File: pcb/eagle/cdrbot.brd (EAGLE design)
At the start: 50 x 50 mm, 28 parts, among them IC1 PIC18F25K50, J1 CON_HEADER_1X06-PTH_M, J12 ICSP, J13 CON_HEADER_1X05-PTH_M, J2 CON_HEADER_1X06-PTH_M, J3 CON_HEADER_1X06-PTH_M, J4 CON_HEADER_1X08-PTH_M, J5 CON_HEADER_1X08-PTH_M, J6 CON_HEADER_1X08-PTH_M, J7 CON_HEADER_1X03-PTH_M, J8 CON_HEADER_1X03-PTH_M, J9 CON_HEADER_1X03-PTH_M, SW1 RESET, SW2 PRG, X1 VIN

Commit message: Nueva version del PCB
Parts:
- removed J7, J8, J9: CON_HEADER_1X03-PTH_M, gary:M1X03_M
- removed JP1: USB-MICROB, SparkFun-Connectors:USB-MICROB
- removed X1: VIN, con-wago-508:W237-132
- added BATERIA, SWITCH: CON_HEADER_1X02-PTH-M, gary:M1X02_M
- added C4, C5: 22pF, gary:C025-025X050
- added SJ1: VBUS, jumper:SJ
- added XTAL1: 20MHz, gary:HC-49UV
- moved C1 5.57 mm to (12.7, 20.3), turned to 180 degrees
- moved R3 4.83 mm to (15.0, 38.1)
- moved ON 3.42 mm to (7.37, 39.1)
- moved RC0 3.30 mm to (18.5, 2.54)
- moved R4 1.37 mm to (18.5, 10.2)
- moved C2 1.27 mm to (32.5, 16.5)
- moved USB1 0.76 mm to (45.2, 13.2)
- moved C3 0.76 mm to (25.4, 1.78)
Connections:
- removed net RA6: IC1.10, J13.4
- removed net RA7: IC1.9, R2.1, SW2.2
- removed net RC1: IC1.12, J9.2
- new net N$2: BATERIA.1, SWITCH.2
- new net OSC1: C5.1, IC1.9, XTAL1.1
- new net OSC2: C4.1, IC1.10, XTAL1.2
- new net VBUS: SJ1.2, USB1.VUSB
- net 5V: now also SJ1.1, SWITCH.1; no longer J8.1, J8.2, J8.3, JP1.VBUS, USB1.VUSB, X1.1
- net D+: no longer JP1.D+
- net D-: no longer JP1.D-
- net GND: now also BATERIA.2, C4.2, C5.2; no longer J7.1, J7.2, J7.3, JP1.GND, JP1.MT1, JP1.MT2, X1.2
- net RB4: now also R2.1, SW2.2
- net RC0: no longer J9.3
- net RC2: now also J13.4; no longer J9.1
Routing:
- net RA7: track 46.3 -> 0.00 mm, vias 2 -> 0
- net GND: track 77.4 -> 39.6 mm, vias 6 -> 22
- net RA6: track 24.2 -> 0.00 mm
- net RB4: track 5.08 -> 24.9 mm
- net OSC1: track 0.00 -> 18.0 mm
- net OSC2: track 0.00 -> 12.1 mm
- net RC2: track 5.08 -> 16.5 mm
- net 5V: track 114.1 -> 105.9 mm
- net D-: track 32.2 -> 26.9 mm
- net RC1: track 5.08 -> 0.00 mm
- net VBUS: track 0.00 -> 3.43 mm
- net PIC_RX: track 19.7 -> 17.0 mm
- net N$2: track 0.00 -> 2.54 mm
- net D+: track 21.3 -> 23.2 mm, vias 2 -> 0
- net RC0: track 5.08 -> 3.57 mm
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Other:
- board text added: "20130507"
- board text removed: "20130423"
- board text removed: "RA6"
- board text removed: "RC0"
- board text removed: "RC1"
- board text removed: "VDD"
- board text removed: "VSS"

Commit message: Generados gerbers para fabricación
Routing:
- net GND: track 39.6 -> 38.3 mm
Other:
- board text added: "CdR"

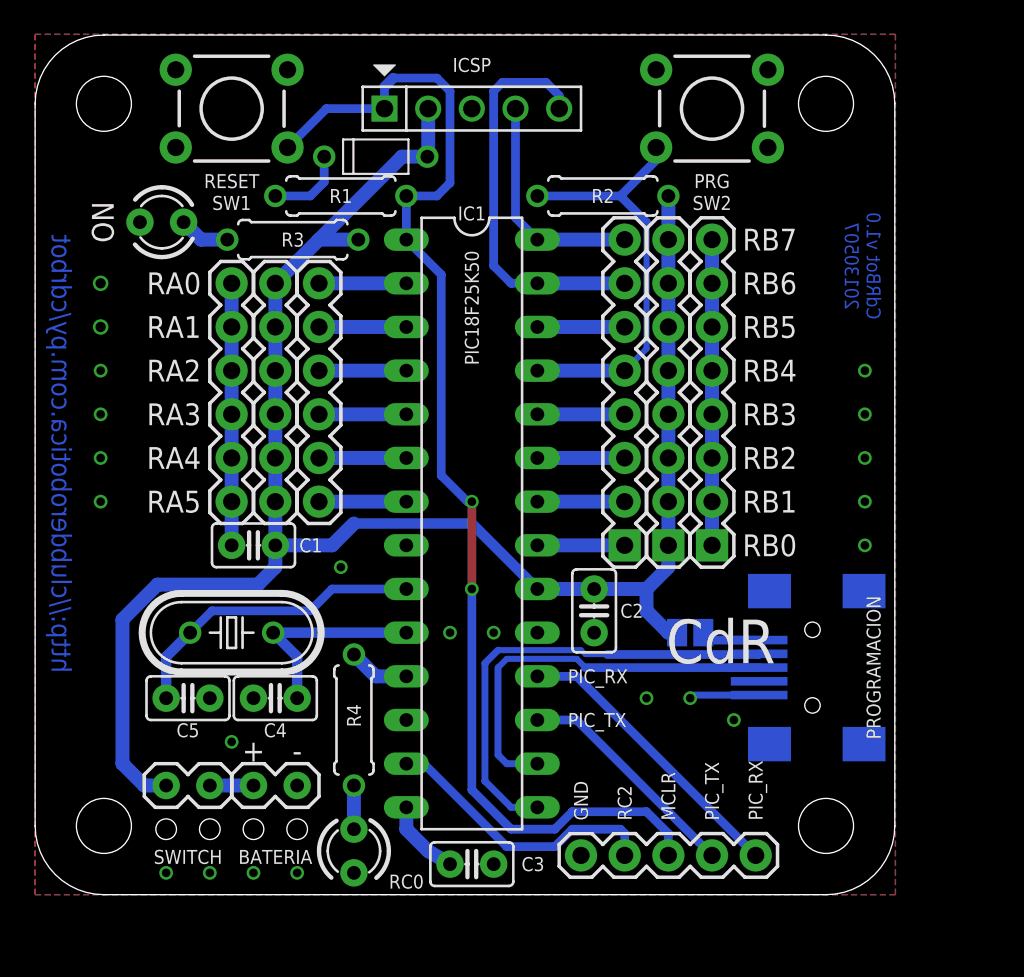
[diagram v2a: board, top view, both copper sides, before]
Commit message: Added On/Off switch, increase cable holes, removed diode
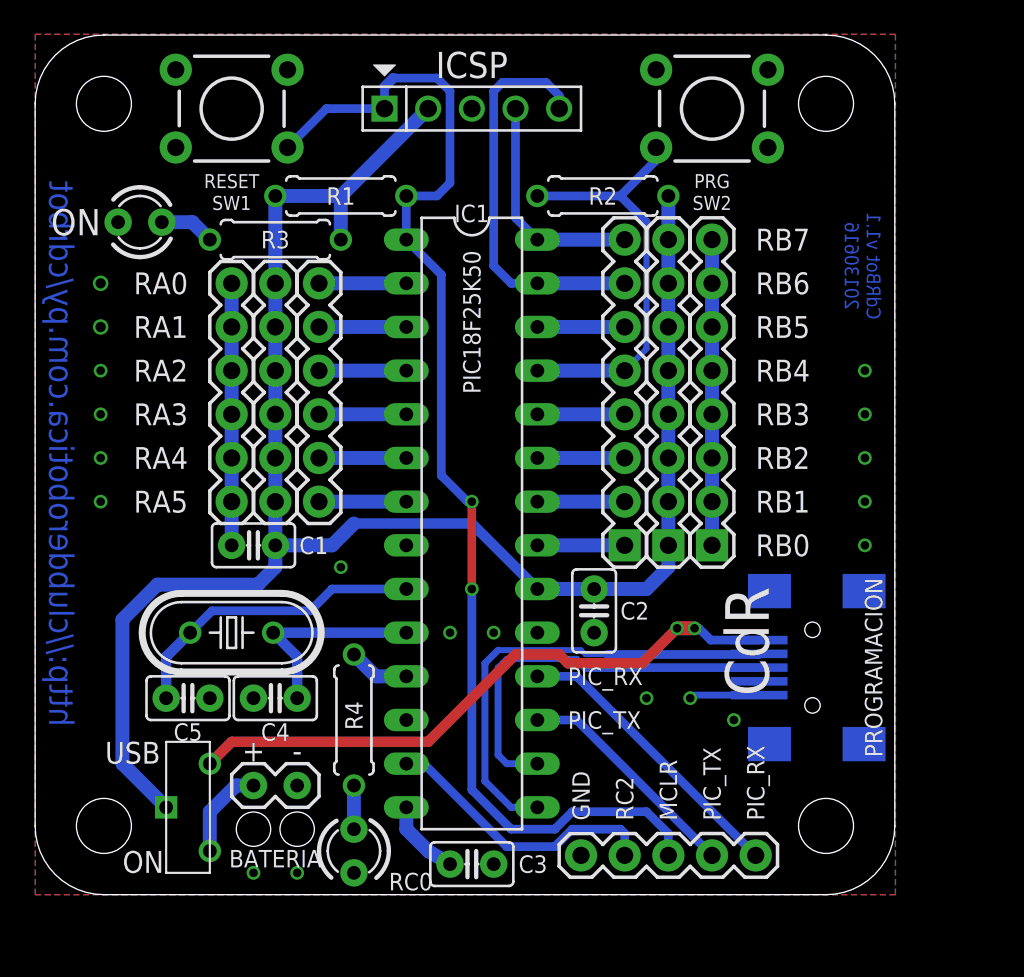
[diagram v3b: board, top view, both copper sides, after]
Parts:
- removed D1: 1N4148, SparkFun:DOIDE-1N4148
- removed SJ1: VBUS, jumper:SJ
- removed SWITCH: CON_HEADER_1X02-PTH-M, gary:M1X02_M
- added S1: 1P2T, gary:1P2T
- moved ON 1.27 mm to (6.10, 39.1)
- moved R3 1.02 mm to (14.0, 38.1)
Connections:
- removed net N$2: BATERIA.1, SWITCH.2
- net 5V: now also R1.2, S1.P$1; no longer D1.A, SJ1.1, SWITCH.1
- net N$1: now also BATERIA.1, S1.P$2; no longer D1.C, R1.2
- net VBUS: now also S1.P$3; no longer SJ1.2
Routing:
- net VBUS: track 3.43 -> 36.9 mm, vias 0 -> 2
- net N$2: track 2.54 -> 0.00 mm
- net 5V: track 105.9 -> 104.5 mm
- net N$1: track 4.65 -> 5.46 mm
- net GND: vias 22 -> 19
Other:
- board text added: "20130616"
- board text added: "CdRBot v1.1"
- board text added: "ON"
- board text added: "USB"
- board text removed: "20130507"
- board text removed: "CdRBot v1.0"

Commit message: Added support fot TSOP38238
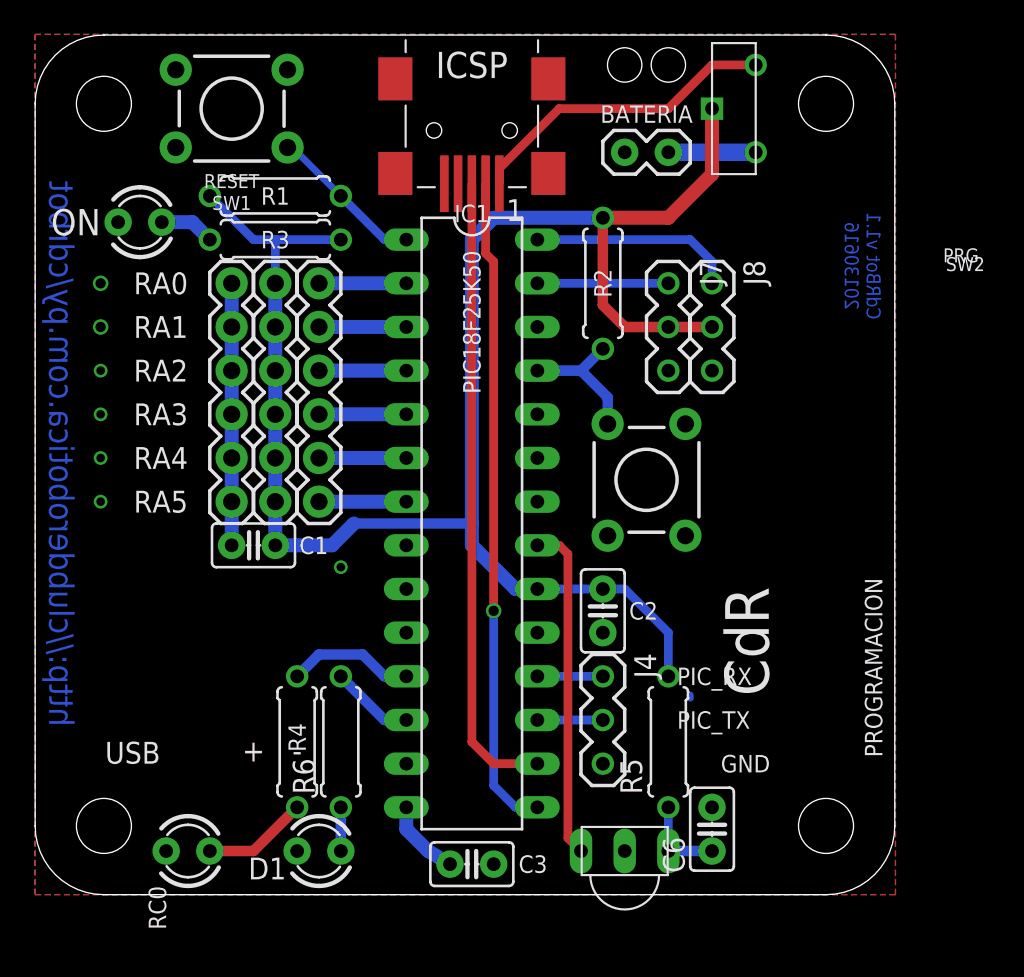
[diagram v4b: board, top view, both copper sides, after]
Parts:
- removed C4, C5: 22pF, gary:C025-025X050
- removed J12: ICSP, dp_devices:HEADER_PRG_1X05_ICSP_B
- removed J13: CON_HEADER_1X05-PTH_M, gary:M1X05_M
- removed J5, J6: CON_HEADER_1X08-PTH_M, gary:M1X08_M
- removed XTAL1: 20MHz, gary:HC-49UV
- added C6: (no value), gary:C025-025X050
- added D1: LED-3MM, gary:LED-3MM
- added IC2: IC_IR_TSOP1838-V, gary:TSOP18XX_V
- added J7, J8: CON_HEADER_1X03-PTH_M, gary:M1X03_M
- added R5, R6: (no value), gary:RTH025W_03
- J4: value CON_HEADER_1X08-PTH_M -> CON_HEADER_1X03-PTH_M; device gary:M1X08_M -> gary:M1X03_M
- moved S1 51.6 mm to (39.4, 45.7)
- moved BATERIA 42.7 mm to (35.6, 43.2), turned to 180 degrees
- moved USB1 37.0 mm to (25.4, 44.5), flipped to the top, turned to 180 degrees
- moved SW2 21.9 mm to (35.6, 24.1), turned to 90 degrees
- moved RC0 9.65 mm to (8.89, 2.54), turned to 180 degrees
- moved J4 7.73 mm to (33.0, 12.7), turned to 270 degrees
- moved R2 5.08 mm to (33.0, 35.6), turned to 90 degrees
- moved R1 3.81 mm to (14.0, 40.6)
- moved R4 3.54 mm to (15.2, 8.89)
- moved C2 0.51 mm to (33.0, 16.5)
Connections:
- removed net OSC1: C5.1, IC1.9, XTAL1.1
- removed net OSC2: C4.1, IC1.10, XTAL1.2
- removed net RB0: IC1.21, J4.1
- removed net RB6: IC1.27, J12.5, J4.7
- removed net RB7: IC1.28, J12.4, J4.8
- new net IRLED: D1.A, R6.1
- new net IR_LED: IC1.12, R6.2
- new net IR_OUT: IC1.21, IC2.OUT
- new net L_SERVO: IC1.27, J7.1
- new net R_SERVO: IC1.28, J8.1
- new net VCC_TSOP: C6.1, IC2.VCC, R5.1
- net 5V: now also J7.2, J8.2, R5.2; no longer J12.2, J5.1, J5.2, J5.3, J5.4, J5.5, J5.6, J5.7, J5.8
- net GND: now also C6.2, D1.K, IC2.GND, J4.3, J7.3, J8.3; no longer C4.2, C5.2, J12.3, J13.5, J6.1, J6.2, J6.3, J6.4, J6.5, J6.6, J6.7, J6.8
- net MCLR_VPP: no longer J12.1, J13.3
- net PIC_RX: now also J4.1; no longer J13.1
- net PIC_TX: now also J4.2; no longer J13.2
- net RB1: no longer J4.2
- net RB2: no longer J4.3
- net RB3: no longer J4.4
- net RB4: no longer J4.5
- net RB5: no longer J4.6
- net RC2: no longer J13.4
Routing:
- net MCLR_VPP: track 71.2 -> 9.13 mm, vias 2 -> 0
- net RB6: track 23.3 -> 0.00 mm
- net GND: track 38.3 -> 15.4 mm, vias 19 -> 7
- net IR_OUT: track 0.00 -> 19.6 mm
- net VBUS: track 36.9 -> 18.3 mm, vias 2 -> 0
- net OSC1: track 18.0 -> 0.00 mm
- net RB4: track 24.9 -> 8.08 mm
- net RC2: track 16.5 -> 0.00 mm
- net D+: track 23.2 -> 36.8 mm
- net RB7: track 13.2 -> 0.00 mm
- net PIC_RX: track 17.0 -> 3.81 mm
- net OSC2: track 12.1 -> 0.00 mm
- net R_SERVO: track 0.00 -> 12.0 mm
- net D-: track 26.9 -> 38.3 mm, vias 0 -> 1
- net PIC_TX: track 13.4 -> 3.81 mm
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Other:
- board text removed: "MCLR"
- board text removed: "ON"
- board text removed: "RB0"
- board text removed: "RB1"
- board text removed: "RB2"
- board text removed: "RB3"
- board text removed: "RB4"
- board text removed: "RB5"
- board text removed: "RB6"
- board text removed: "RB7"
- board text removed: "RC2"
